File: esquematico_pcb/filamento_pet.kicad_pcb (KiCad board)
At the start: 2 copper layers, 17.8 x 43.2 mm, 6 parts, among them P1 Digital, P2 Analog, P3 CONN_01X01, P4 CONN_01X01, P5 CONN_01X01, P6 CONN_01X01

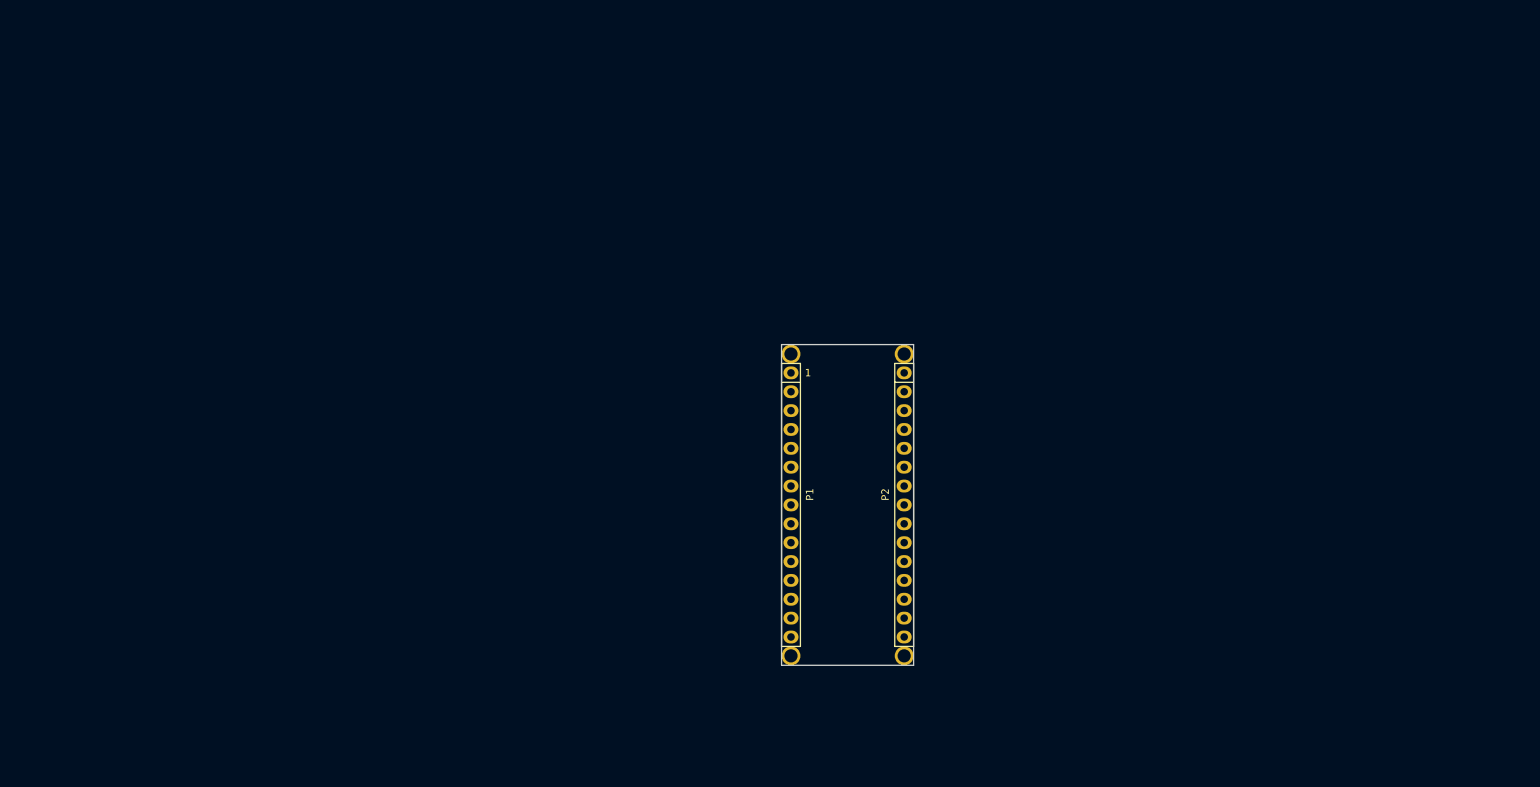
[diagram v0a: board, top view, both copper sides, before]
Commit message: Version sin footprints, necesario para merge
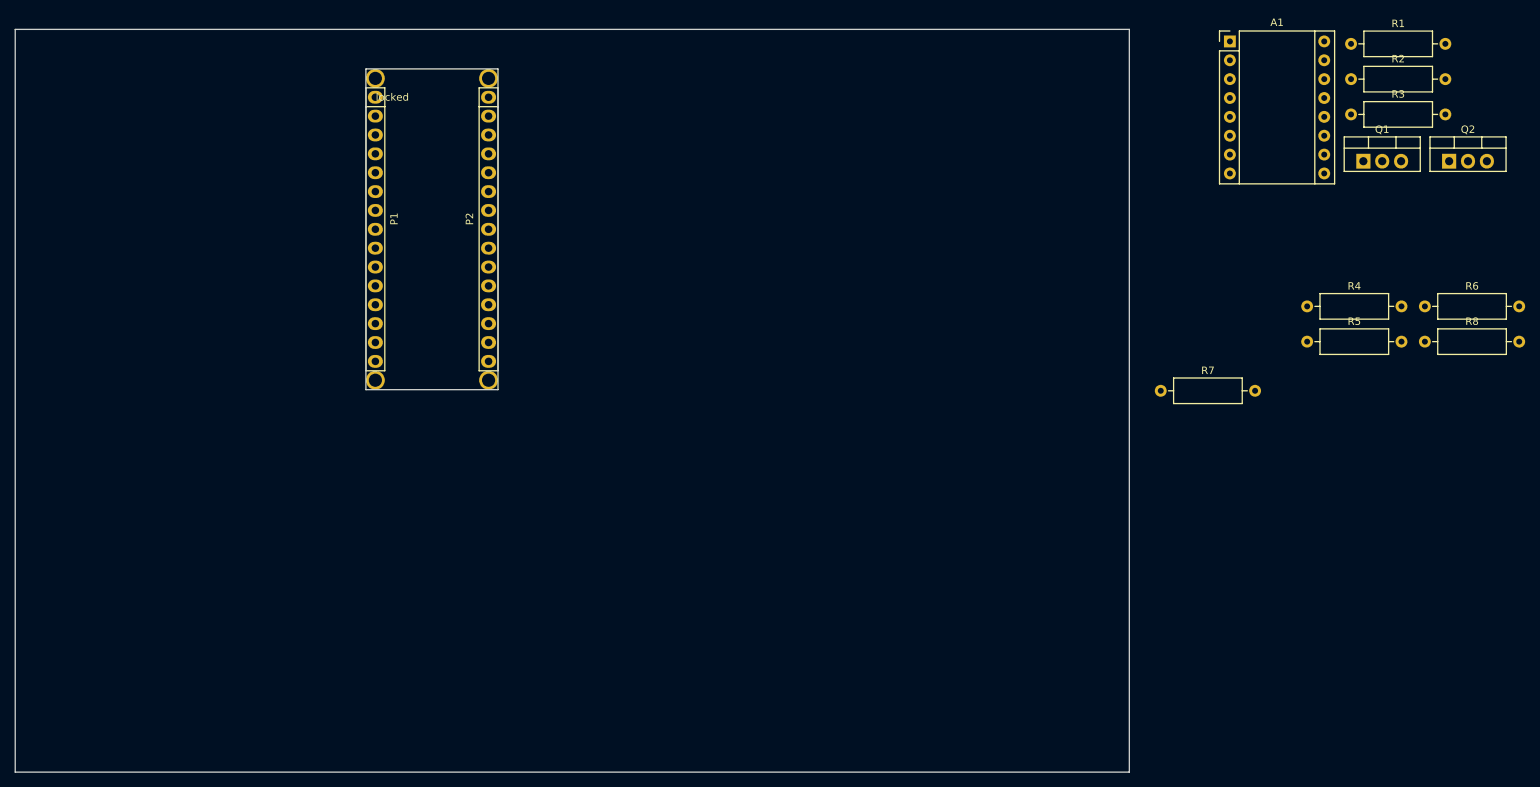
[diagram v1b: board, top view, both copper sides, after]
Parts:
- added A1: Pololu_A4988, Module:Pololu_Breakout-16_15.2x20.3mm, F.Cu at (198.5, 26.6)
- added Q1: IRF540N, Package_TO_SOT_THT:TO-220-3_Vertical, F.Cu at (216.5, 42.7)
- added Q2: IRF540N, Package_TO_SOT_THT:TO-220-3_Vertical, F.Cu at (228.1, 42.7)
- added R1: 1.8K, Resistor_THT:R_Axial_DIN0309_L9.0mm_D3.2mm_P12.70mm_Horizontal, F.Cu at (214.8, 26.9)
- added R2: 10R, Resistor_THT:R_Axial_DIN0309_L9.0mm_D3.2mm_P12.70mm_Horizontal, F.Cu at (214.8, 31.7)
- added R3: 10K, Resistor_THT:R_Axial_DIN0309_L9.0mm_D3.2mm_P12.70mm_Horizontal, F.Cu at (214.8, 36.4)
- added R4: 1.8K, Resistor_THT:R_Axial_DIN0309_L9.0mm_D3.2mm_P12.70mm_Horizontal, F.Cu at (208.9, 62.3)
- added R5: 10R, Resistor_THT:R_Axial_DIN0309_L9.0mm_D3.2mm_P12.70mm_Horizontal, F.Cu at (208.9, 67.0)
- added R6: 10K, Resistor_THT:R_Axial_DIN0309_L9.0mm_D3.2mm_P12.70mm_Horizontal, F.Cu at (224.8, 62.3)
- added R7: 4.7K, Resistor_THT:R_Axial_DIN0309_L9.0mm_D3.2mm_P12.70mm_Horizontal, F.Cu at (189.2, 73.7)
- added R8: 10K, Resistor_THT:R_Axial_DIN0309_L9.0mm_D3.2mm_P12.70mm_Horizontal, F.Cu at (224.8, 67.0)
- moved P1 67.1 mm to (83.5, 34.1)
- moved P2 67.1 mm to (98.7, 34.1)
- moved P5 67.1 mm to (98.7, 72.2)
- moved P6 67.1 mm to (98.7, 31.6)
- moved P3 67.1 mm to (83.5, 31.6)
- moved P4 67.1 mm to (83.5, 72.2)
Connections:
- net /10(**/SS) renamed BUT2
- net /11(**/MOSI) renamed BUT3
- net /7 renamed BUT1
- net /A1 renamed Pote_vel
- net /A4 renamed SDA
- net /A5 renamed SCL
- P1 pad 5: /2 -> EN
- P1 pad 6: /3(**) -> STEP
- P1 pad 7: /4 -> DIR
- P1 pad 8: /5(**) -> MOS
- P1 pad 9: /6(**) -> FAN
- P2 pad 12: /A0 -> Thermistor
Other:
- board size 17.8 x 43.2 mm -> 150 x 100 mm
- net class Default removed
- board text added: "locked"
- board text removed: "1"
